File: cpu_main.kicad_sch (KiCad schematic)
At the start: 18 parts, among them Q1 9018G, U1 Z80, U10 2764, U2 74LS244, U3 74LS257, U4 74LS257, U5 74LS00, U6 27128, U7 27128/27256, U8 GA1, U9 74LS273

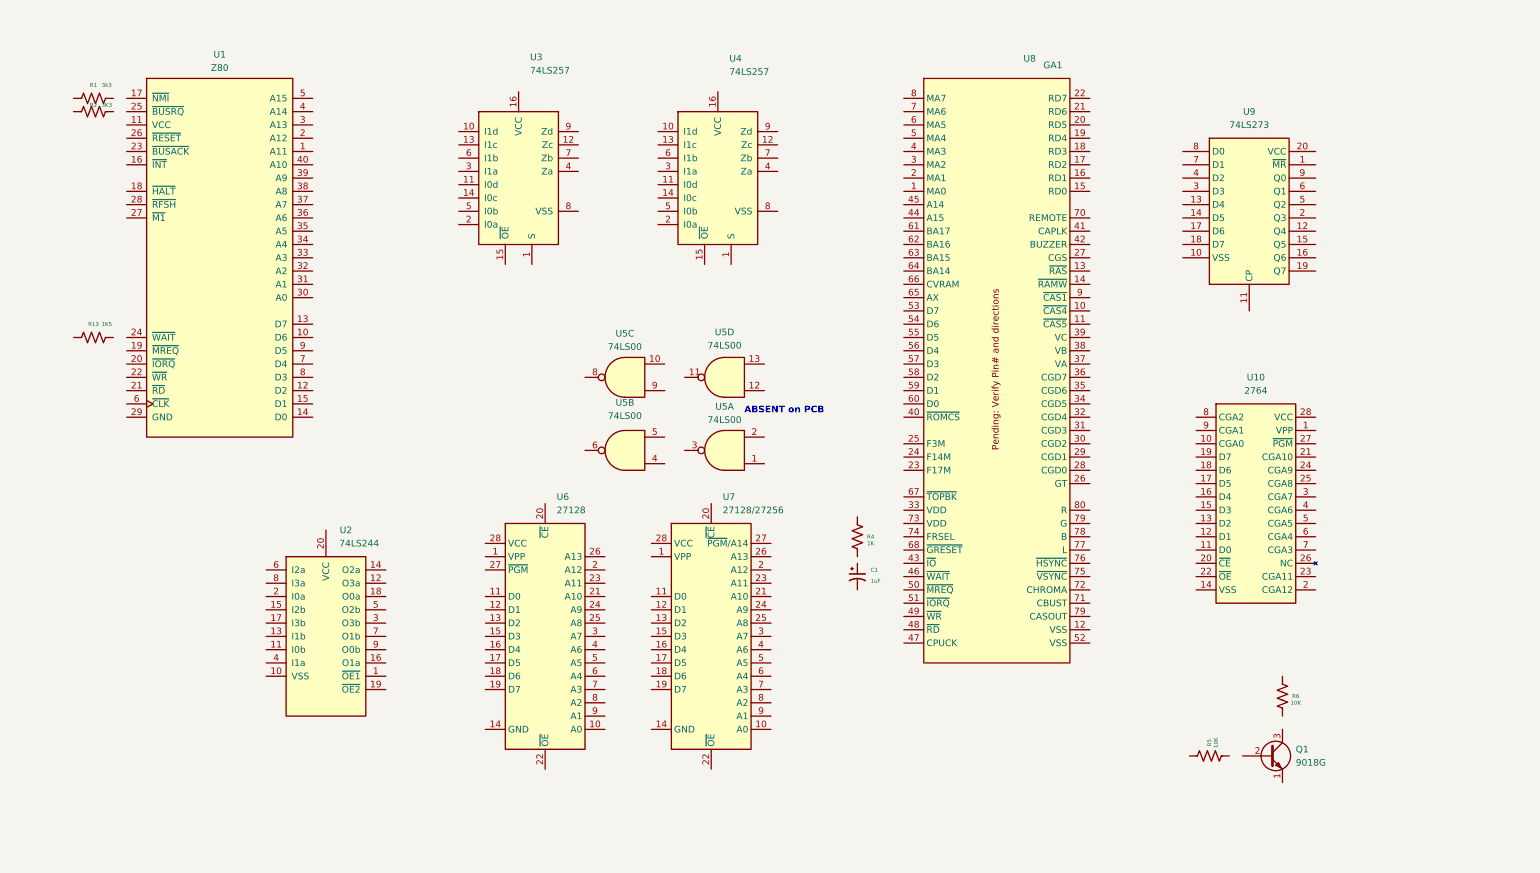
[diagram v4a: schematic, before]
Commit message: Started A[0..15] and MA[0..7] on main circuit
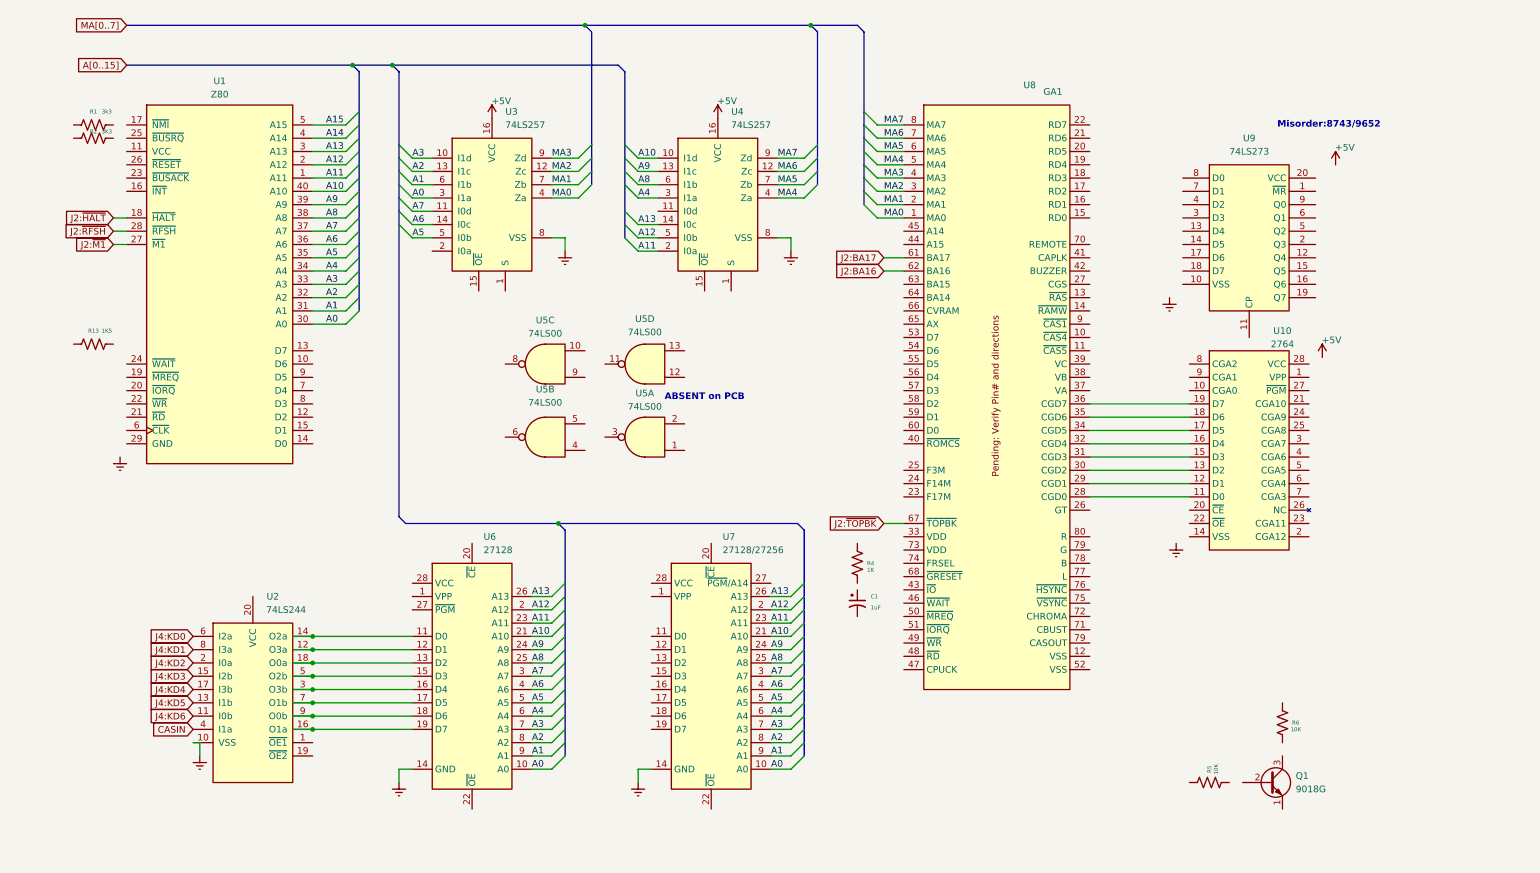
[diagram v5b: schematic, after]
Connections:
- net A3: now reaches U3.10 (I1d)
- net A3: now also U1.33 (A3), U6.7 (A3), U7.7 (A3)
- net A7: now reaches U3.11 (I0d)
- net A7: now also U1.37 (A7), U6.3 (A7), U7.3 (A7)
- net MA2: now reaches U3.12 (Zc)
- net MA2: now also U8.3 (MA2)
- net A2: now reaches U3.13 (I1c)
- net A2: now also U1.32 (A2), U6.8 (A2), U7.8 (A2)
- net A6: now reaches U3.14 (I0c)
- net A6: now also U1.36 (A6), U6.4 (A6), U7.4 (A6)
- net +5V: now reaches U3.16 (VCC)
- net +5V: now also U4.16 (VCC)
- net A0: now reaches U3.3 (I1a)
- net A0: now also U1.30 (A0), U6.10 (A0), U7.10 (A0)
- net MA0: now reaches U3.4 (Za)
- net MA0: now also U8.1 (MA0)
- net A5: now reaches U3.5 (I0b)
- net A5: now also U1.35 (A5), U6.5 (A5), U7.5 (A5)
- net A1: now reaches U3.6 (I1b)
- net A1: now also U1.31 (A1), U6.9 (A1), U7.9 (A1)
- net MA1: now reaches U3.7 (Zb)
- net MA1: now also U8.2 (MA1)
- net MA3: now reaches U3.9 (Zd)
- net MA3: now also U8.4 (MA3)
- net A12: now reaches U7.2 (A12)
- net A12: now also U1.2 (A12), U4.5 (I0b), U6.2 (A12)
- net A10: now reaches U7.21 (A10)
- net A10: now also U1.40 (A10), U4.10 (I1d), U6.21 (A10)
- net A11: now reaches U7.23 (A11)
- net A11: now also U1.1 (A11), U4.2 (I0a), U6.23 (A11)
- net A9: now reaches U7.24 (A9)
- net A9: now also U1.39 (A9), U4.13 (I1c), U6.24 (A9)
- net A8: now reaches U7.25 (A8)
- net A8: now also U1.38 (A8), U4.6 (I1b), U6.25 (A8)
- net A13: now reaches U7.26 (A13)
- net A13: now also U1.3 (A13), U4.14 (I0c), U6.26 (A13)
- net A4: now reaches U7.6 (A4)
- net A4: now also U1.34 (A4), U4.3 (I1a), U6.6 (A4)
- net J4:KD6: now reaches U2.11 (I0b)
- net at U2.12 (O3a): now also U6.12 (D1)
- net J4:KD5: now reaches U2.13 (I1b)
- net at U2.14 (O2a): now also U6.11 (D0)
- net J4:KD3: now reaches U2.15 (I2b)
- net at U2.16 (O1a): now also U6.19 (D7)
- net J4:KD4: now reaches U2.17 (I3b)
- net at U2.18 (O0a): now also U6.13 (D2)
- net J4:KD2: now reaches U2.2 (I0a)
- net at U2.3 (O3b): now also U6.16 (D4)
- net CASIN: now reaches U2.4 (I1a)
- net at U2.5 (O2b): now also U6.15 (D3)
- net J4:KD0: now reaches U2.6 (I2a)
- net at U2.7 (O1b): now also U6.17 (D5)
- net J4:KD1: now reaches U2.8 (I3a)
- net at U2.9 (O0b): now also U6.18 (D6)
- net at U10.11 (D0): now also U8.28 (CGD0)
- net at U10.12 (D1): now also U8.29 (CGD1)
- net at U10.13 (D2): now also U8.30 (CGD2)
- net at U10.15 (D3): now also U8.31 (CGD3)
- net at U10.16 (D4): now also U8.32 (CGD4)
- net at U10.17 (D5): now also U8.34 (CGD5)
- net at U10.18 (D6): now also U8.35 (CGD6)
- net at U10.19 (D7): now also U8.36 (CGD7)
- net J2:~{HALT}: now reaches U1.18 (~{HALT})
- net J2:~{M1}: now reaches U1.27 (~{M1})
- net J2:~{RFSH}: now reaches U1.28 (~{RFSH})
- net A14: now reaches U1.4 (A14)
- net A15: now reaches U1.5 (A15)
- net MA6: now reaches U4.12 (Zc)
- net MA6: now also U8.7 (MA6)
- net MA4: now reaches U4.4 (Za)
- net MA4: now also U8.5 (MA4)
- net MA5: now reaches U4.7 (Zb)
- net MA5: now also U8.6 (MA5)
- net MA7: now reaches U4.9 (Zd)
- net MA7: now also U8.8 (MA7)
- net J2:BA17: now reaches U8.61 (BA17)
- net J2:BA16: now reaches U8.62 (BA16)
- net J2:~{TOPBK}: now reaches U8.67 (~{TOPBK})
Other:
- note added: "Misorder:8743/9652"
- title: Main Circuit -> Laser 500 (PAL) Main Circuit
- moved on the sheet: C1, Q1, R1, R13, R2, R4, R5, R6, U1, U10, U2, U3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

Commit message: Main circuit : Finished most of the buses
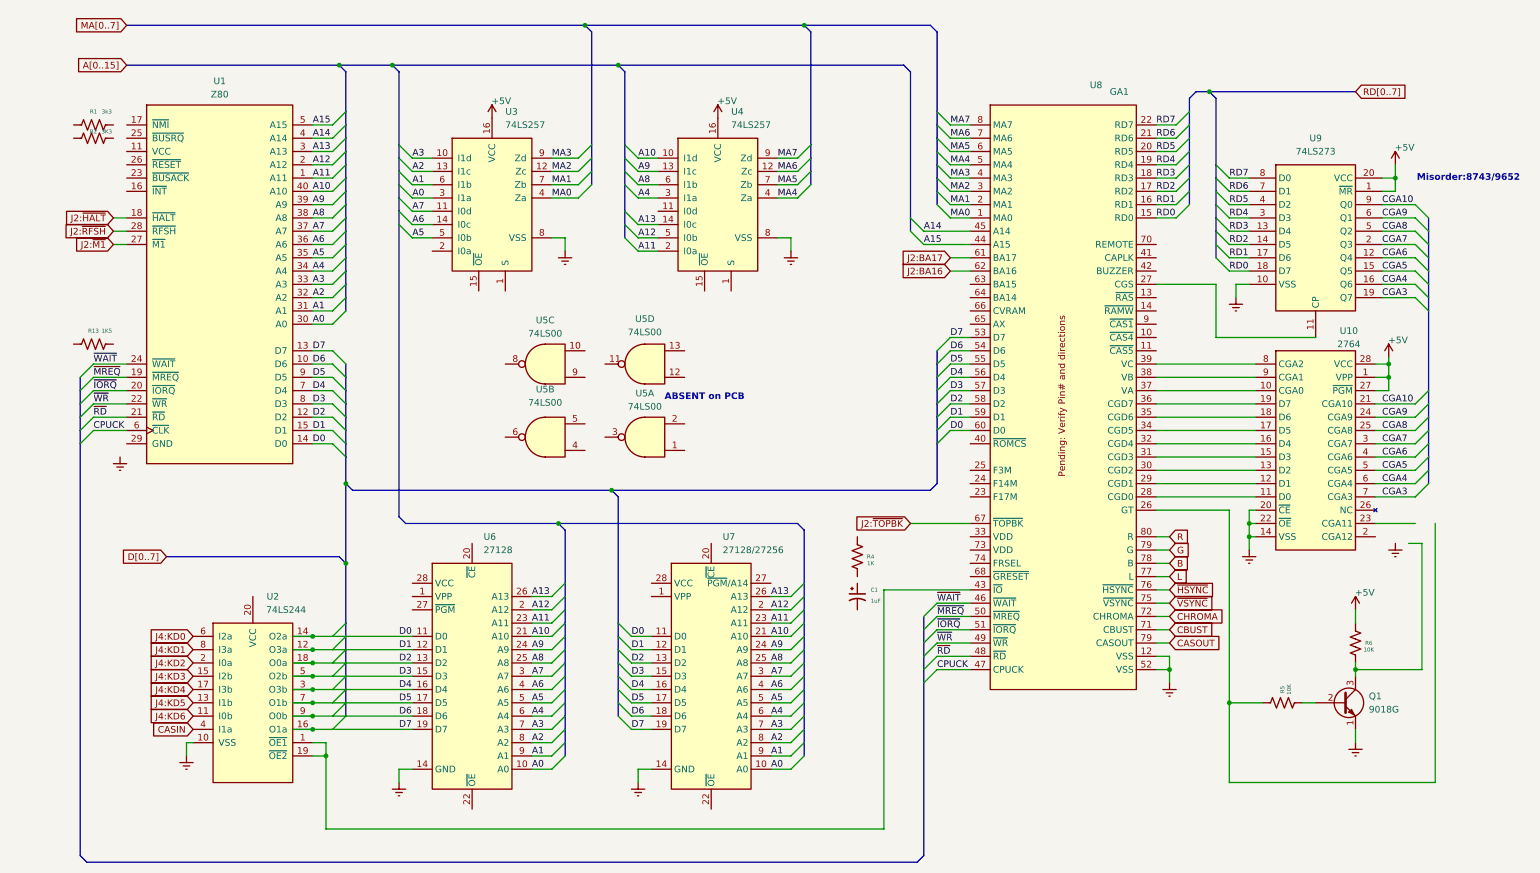
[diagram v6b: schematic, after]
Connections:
- net +5V: now also R6.2, U10.1 (VPP), U10.27 (~{PGM}), U10.28 (VCC), U9.1 (~{MR}), U9.20 (VCC)
- net A14: now also U8.45 (A14)
- net A15: now also U8.44 (A15)
- net at U9.11 (CP): now also U8.27 (CGS)
- net CGA6: now reaches U9.12 (Q4)
- net CGA6: now also U10.4 (CGA6)
- net RD3: now reaches U9.13 (D4)
- net RD3: now also U8.18 (RD3)
- net RD2: now reaches U9.14 (D5)
- net RD2: now also U8.17 (RD2)
- net CGA5: now reaches U9.15 (Q5)
- net CGA5: now also U10.5 (CGA5)
- net CGA4: now reaches U9.16 (Q6)
- net CGA4: now also U10.6 (CGA4)
- net RD1: now reaches U9.17 (D6)
- net RD1: now also U8.16 (RD1)
- net RD0: now reaches U9.18 (D7)
- net RD0: now also U8.15 (RD0)
- net CGA3: now reaches U9.19 (Q7)
- net CGA3: now also U10.7 (CGA3)
- net CGA7: now reaches U9.2 (Q3)
- net CGA7: now also U10.3 (CGA7)
- net RD4: now reaches U9.3 (D3)
- net RD4: now also U8.19 (RD4)
- net RD5: now reaches U9.4 (D2)
- net RD5: now also U8.20 (RD5)
- net CGA8: now reaches U9.5 (Q2)
- net CGA8: now also U10.25 (CGA8)
- net CGA9: now reaches U9.6 (Q1)
- net CGA9: now also U10.24 (CGA9)
- net RD6: now reaches U9.7 (D1)
- net RD6: now also U8.21 (RD6)
- net RD7: now reaches U9.8 (D0)
- net RD7: now also U8.22 (RD7)
- net CGA10: now reaches U9.9 (Q0)
- net CGA10: now also U10.21 (CGA10)
- net D0: now reaches U7.11 (D0)
- net D0: now also U1.14 (D0), U2.14 (O2a), U6.11 (D0), U8.60 (D0)
- net D1: now reaches U7.12 (D1)
- net D1: now also U1.15 (D1), U2.12 (O3a), U6.12 (D1), U8.59 (D1)
- net D2: now reaches U7.13 (D2)
- net D2: now also U1.12 (D2), U2.18 (O0a), U6.13 (D2), U8.58 (D2)
- net D3: now reaches U7.15 (D3)
- net D3: now also U1.8 (D3), U2.5 (O2b), U6.15 (D3), U8.57 (D3)
- net D4: now reaches U7.16 (D4)
- net D4: now also U1.7 (D4), U2.3 (O3b), U6.16 (D4), U8.56 (D4)
- net D5: now reaches U7.17 (D5)
- net D5: now also U1.9 (D5), U2.7 (O1b), U6.17 (D5), U8.55 (D5)
- net D6: now reaches U7.18 (D6)
- net D6: now also U1.10 (D6), U2.9 (O0b), U6.18 (D6), U8.54 (D6)
- net D7: now reaches U7.19 (D7)
- net D7: now also U1.13 (D7), U2.16 (O1a), U6.19 (D7), U8.53 (D7)
- net at U2.1 (~{OE1}): now also U2.19 (~{OE2}), U8.43 (~{IO})
- net at R6.1: now also Q1.3 (C)
- net at Q1.2 (B): now also R5.1
- net at U10.10 (CGA0): now also U8.37 (VA)
- net at U10.14 (VSS): now also U10.20 (~{CE}), U10.22 (~{OE})
- net at U10.8 (CGA2): now also U8.39 (VC)
- net at U10.9 (CGA1): now also U8.38 (VB)
- net ~{MREQ}: now reaches U1.19 (~{MREQ})
- net ~{MREQ}: now also U8.50 (~{MREQ})
- net ~{IORQ}: now reaches U1.20 (~{IORQ})
- net ~{IORQ}: now also U8.51 (~{IORQ})
- net ~{RD}: now reaches U1.21 (~{RD})
- net ~{RD}: now also U8.48 (~{RD})
- net ~{WR}: now reaches U1.22 (~{WR})
- net ~{WR}: now also U8.49 (~{WR})
- net ~{WAIT}: now reaches U1.24 (~{WAIT})
- net ~{WAIT}: now also U8.46 (~{WAIT})
- net CPUCK: now reaches U1.6 (~{CLK})
- net CPUCK: now also U8.47 (CPUCK)
- net at R5.2: now also U8.26 (GT)
- net at U8.12 (VSS): now also U8.52 (VSS)
- net CBUST: now reaches U8.71 (CBUST)
- net CHROMA: now reaches U8.72 (CHROMA)
- net ~{VSYNC}: now reaches U8.75 (~{VSYNC})
- net ~{HSYNC}: now reaches U8.76 (~{HSYNC})
- net L: now reaches U8.77 (L)
- net B: now reaches U8.78 (B)
- net G: now reaches U8.79 (G)
- net R: now reaches U8.80 (R)
- new net CASOUT: U8.79 (G)
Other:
- moved on the sheet: C1, Q1, R4, R5, R6, U10, U8, U9

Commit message: End of vacation
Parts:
- removed U1: Z80, symbol Laser500:Z80
- removed U10: 2764, Package_DIP:DIP-28_W15.24mm, symbol Laser500:2764
- removed U2: 74LS244, symbol Laser500:74LS244
- added U1: Z80, symbol CPU:Z80CPU
- added U2: 74LS244, symbol 74xx:74LS244
- added U21: 2764, Package_DIP:DIP-28_W15.24mm, symbol Memory_EPROM:2764
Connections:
- net +5V: now also R1.2, R13.2, R2.2, R4.2, U8.33 (VDD), U8.73 (VDD), U8.74 (FRSEL), U1.11 (VCC), U2.20 (VCC), U21.1 (VPP), U21.27 (~{PGM}), U21.28 (VCC)
- net A0: now also U1.30 (A0)
- net A1: now also U1.31 (A1)
- net A10: now also U1.40 (A10)
- net A11: now also U1.1 (A11)
- net A12: now also U1.2 (A12)
- net A13: now also U1.3 (A13)
- net A14: now also U1.4 (A14)
- net A15: now also U1.5 (A15)
- net A2: now also U1.32 (A2)
- net A3: now also U1.33 (A3)
- net A4: now also U1.34 (A4)
- net A5: now also U1.35 (A5)
- net A6: now also U1.36 (A6)
- net A7: now also U1.37 (A7)
- net A8: now also U1.38 (A8)
- net A9: now also U1.39 (A9)
- net CASIN: now also U2.4 (I1a)
- net CGA10: now also U21.21 (CGA10)
- net CGA3: now also U21.7 (CGA3)
- net CGA4: now also U21.6 (CGA4)
- net CGA5: now also U21.5 (CGA5)
- net CGA6: now also U21.4 (CGA6)
- net CGA7: now also U21.3 (CGA7)
- net CGA8: now also U21.25 (CGA8)
- net CGA9: now also U21.24 (CGA9)
- net CPUCK: now also U1.6 (~{CLK})
- net D0: now also U1.14 (D0), U2.14 (O2a)
- net D1: now also U1.15 (D1), U2.12 (O3a)
- net D2: now also U1.12 (D2), U2.18 (O0a)
- net D3: now also U1.8 (D3), U2.5 (O2b)
- net D4: now also U1.7 (D4), U2.3 (O3b)
- net D5: now also U1.9 (D5), U2.7 (O1b)
- net D6: now also U1.10 (D6), U2.9 (O0b)
- net D7: now also U1.13 (D7), U2.16 (O1a)
- net J2:~{HALT}: now also U1.18 (~{HALT})
- net J2:~{M1}: now also U1.27 (~{M1})
- net J2:~{RFSH}: now also U1.28 (~{RFSH})
- net J4:KD0: now also U2.6 (I2a)
- net J4:KD1: now also U2.8 (I3a)
- net J4:KD2: now also U2.2 (I0a)
- net J4:KD3: now also U2.15 (I2b)
- net J4:KD4: now also U2.17 (I3b)
- net J4:KD5: now also U2.13 (I1b)
- net J4:KD6: now also U2.11 (I0b)
- net ~{IORQ}: now also U1.20 (~{IORQ})
- net ~{MREQ}: now also U1.19 (~{MREQ})
- net ~{RD}: now also U6.22 (~{OE}), U7.22 (~{OE}), U8.43 (~{IO}), U1.21 (~{RD}), U2.1 (OE1), U2.19 (OE2)
- net ~{WAIT}: now also R13.1, U1.24 (~{WAIT})
- net ~{WR}: now also U1.22 (~{WR})
- net at U3.1 (S): now also U4.1 (S), U8.65 (AX)
- net at U3.15 (~{OE}): now also U4.15 (~{OE}), U8.66 (CVRAM)
- net at U3.2 (I0a): now also U8.64 (BA14)
- net at C1.1: now also R4.1, U8.68 (~{GRESET})
- net at R1.1: now also U1.17 (~{NMI})
- net at U8.37 (VA): now also U21.10 (CGA0)
- net at U8.28 (CGD0): now also U21.11 (D0)
- net at U8.29 (CGD1): now also U21.12 (D1)
- net at U8.30 (CGD2): now also U21.13 (D2)
- net at U8.31 (CGD3): now also U21.15 (D3)
- net at U8.32 (CGD4): now also U21.16 (D4)
- net at U8.34 (CGD5): now also U21.17 (D5)
- net at U8.35 (CGD6): now also U21.18 (D6)
- net at U8.36 (CGD7): now also U21.19 (D7)
- net at U8.39 (VC): now also U21.8 (CGA2)
- net at U8.38 (VB): now also U21.9 (CGA1)
- net at U4.11 (I0d): now also U8.63 (BA15)
- net at R2.1: now also U1.25 (~{BUSRQ})
- net ~{RAS}: now reaches U8.13 (~{RAS})
- net BUZZER: now reaches U8.42 (BUZZER)
- new net: U21.14 (VSS), U21.20 (~{CE}), U21.22 (~{OE})
- no-connect marks 0 -> 1
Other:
- moved on the sheet: C1, Q1, R1, R13, R2, R4, R5, R6, U3, U4, U5A, U5B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
